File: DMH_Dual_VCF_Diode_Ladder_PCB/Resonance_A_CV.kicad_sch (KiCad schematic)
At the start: 24 parts, among them Q1 BC548, Q2 BC548, U3 TL074

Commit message: Reannotated whole schematic
OpAmp annotation is still tentative.
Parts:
- removed R27, R28, R31: 20k, Resistor_THT:R_Axial_DIN0207_L6.3mm_D2.5mm_P7.62mm_Horizontal, symbol Device:R_US
- removed R29, R35, R37, R38, R39, R44: 100k, Resistor_THT:R_Axial_DIN0207_L6.3mm_D2.5mm_P7.62mm_Horizontal, symbol Device:R_US
- removed R30, R34, R42: 10k, Resistor_THT:R_Axial_DIN0207_L6.3mm_D2.5mm_P7.62mm_Horizontal, symbol Device:R_US
- removed R33: 1k, Resistor_THT:R_Axial_DIN0207_L6.3mm_D2.5mm_P7.62mm_Horizontal, symbol Device:R_US
- removed R36: 33k, Resistor_THT:R_Axial_DIN0207_L6.3mm_D2.5mm_P7.62mm_Horizontal, symbol Device:R_US
- removed R40, R41: 100R, Resistor_THT:R_Axial_DIN0207_L6.3mm_D2.5mm_P7.62mm_Horizontal, symbol Device:R_US
- removed R43: 82k, Resistor_THT:R_Axial_DIN0207_L6.3mm_D2.5mm_P7.62mm_Horizontal, symbol Device:R_US
- removed RV10: 100k, Potentiometer_THT:Potentiometer_Bourns_3296W_Vertical, symbol Device:R_Potentiometer_Trim_US
- removed RV11: 100k, SynthStuff:Potentiometer_TT_P110KH1, symbol Device:R_Potentiometer_US
- removed RV8: 100k, SynthStuff:Potentiometer_Alpha_RD901F-40-00D_Single_Vertical, symbol Device:R_Potentiometer_US
- removed RV9: 50k, Potentiometer_THT:Potentiometer_Bourns_3296W_Vertical, symbol Device:R_Potentiometer_Trim_US
- removed U3: TL074, Package_DIP:DIP-14_W7.62mm_Socket, symbol Amplifier_Operational:TL074
- added R62: 33k, Resistor_THT:R_Axial_DIN0207_L6.3mm_D2.5mm_P7.62mm_Horizontal, symbol Device:R_US
- added R63, R72, R73: 20k, Resistor_THT:R_Axial_DIN0207_L6.3mm_D2.5mm_P7.62mm_Horizontal, symbol Device:R_US
- added R64, R65, R67, R71, R76, R77: 100k, Resistor_THT:R_Axial_DIN0207_L6.3mm_D2.5mm_P7.62mm_Horizontal, symbol Device:R_US
- added R66: 82k, Resistor_THT:R_Axial_DIN0207_L6.3mm_D2.5mm_P7.62mm_Horizontal, symbol Device:R_US
- added R68, R70: 100R, Resistor_THT:R_Axial_DIN0207_L6.3mm_D2.5mm_P7.62mm_Horizontal, symbol Device:R_US
- added R69, R74, R75: 10k, Resistor_THT:R_Axial_DIN0207_L6.3mm_D2.5mm_P7.62mm_Horizontal, symbol Device:R_US
- added R78: 1k, Resistor_THT:R_Axial_DIN0207_L6.3mm_D2.5mm_P7.62mm_Horizontal, symbol Device:R_US
- added RV16: 100k, SynthStuff:Potentiometer_TT_P110KH1, symbol Device:R_Potentiometer_US
- added RV17: 50k, Potentiometer_THT:Potentiometer_Bourns_3296W_Vertical, symbol Device:R_Potentiometer_Trim_US
- added RV18: 100k, SynthStuff:Potentiometer_Alpha_RD901F-40-00D_Single_Vertical, symbol Device:R_Potentiometer_US
- added RV19: 100k, Potentiometer_THT:Potentiometer_Bourns_3296W_Vertical, symbol Device:R_Potentiometer_Trim_US
- added U3, U4: TL074, Package_DIP:DIP-14_W7.62mm_Socket, symbol Amplifier_Operational:TL074
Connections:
- net +12V: now also R63.2, R72.2, R73.2, RV19.3
- net -12V: now also RV19.1
- net GND: now also R68.1, R70.1, R76.2, RV16.1, RV18.1, U4.12 (+)
- net Input: now also R67.2
- net Output: now also R78.1
- net Res CV Input: now also R62.1, RV16.3
- net at Q2.1 (C): now also R73.1, R75.2
- net at Q1.2 (B): now also R67.1, R68.2
- net at Q1.3 (E), Q2.3 (E): now also R69.2
- net at Q2.2 (B): now also R70.2, R71.2
- net at Q1.1 (C): now also R72.1, R74.2
- new net: R64.2, R65.2, R66.1, U4.13 (-)
- new net: R66.2, R69.1, U4.14
- new net: R62.2, RV17.1, U3.2 (-)
- new net: R64.1, RV17.2, RV17.3, U3.1
- new net: R65.1, RV18.2
- new net: R75.1, R76.1, U4.10 (+)
- new net: R77.1, R78.2, U4.8
- new net: R71.1, RV19.2
- new net: R74.1, R77.2, U4.9 (-)
- new net: RV16.2, U3.3 (+)
- new net: R63.1, RV18.3

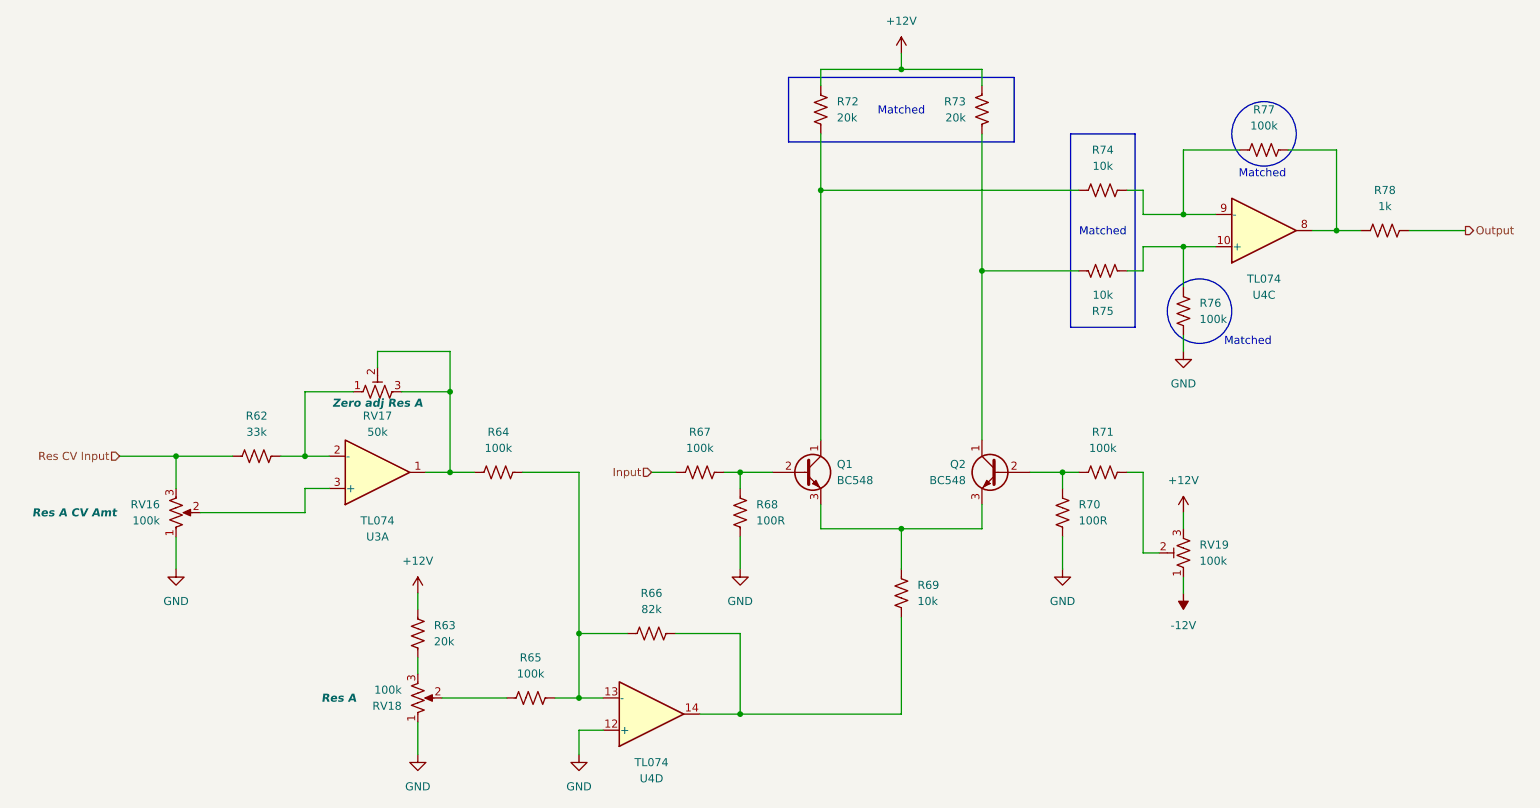
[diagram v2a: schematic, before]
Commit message: Reannotated OpAmps and cleared errors
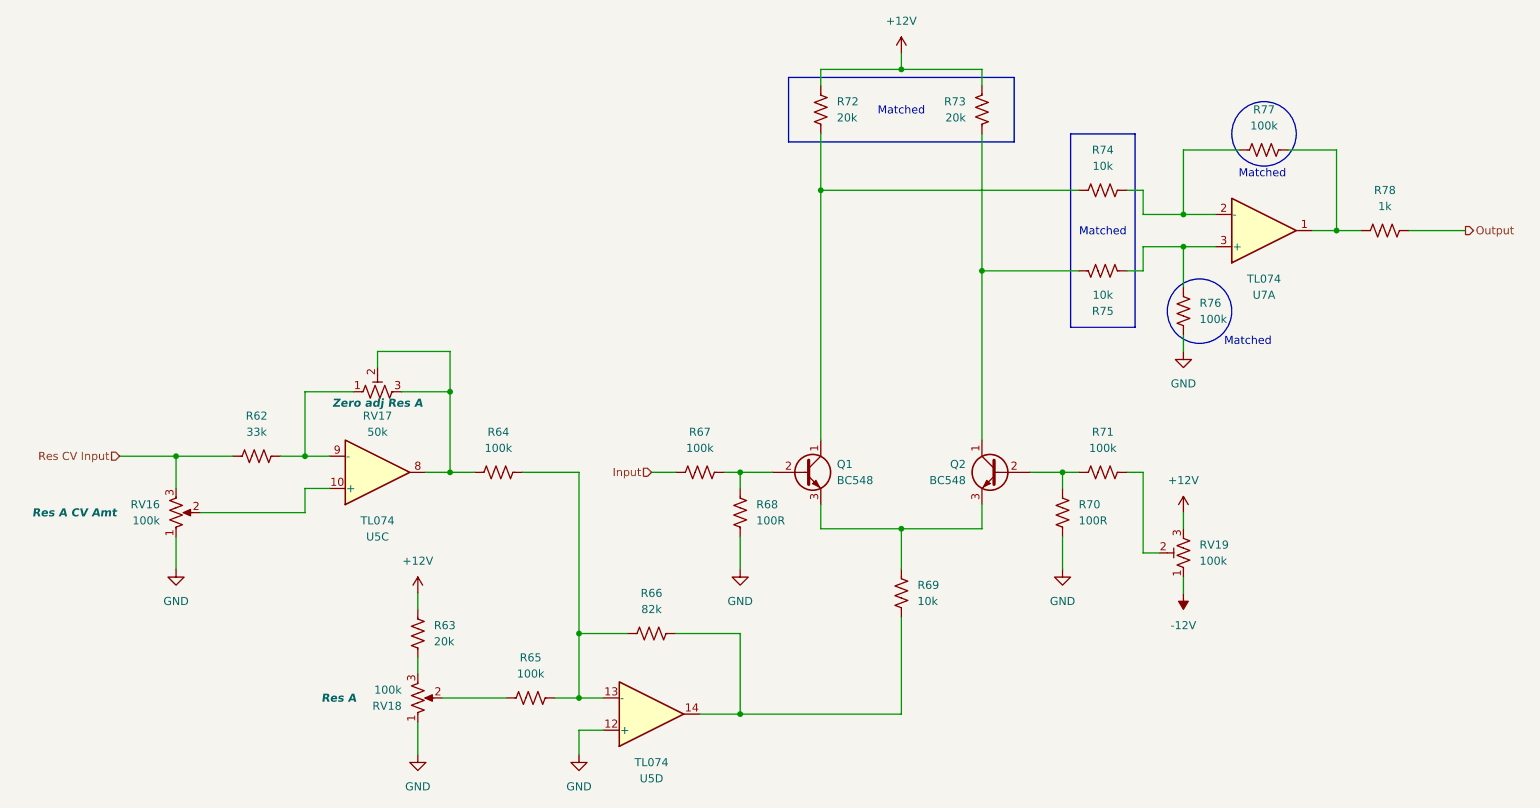
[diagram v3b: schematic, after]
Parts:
- renumbered U4 to U5, U3 to U5, U4 to U7
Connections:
- net at R62.2, RV17.1: now also U5.9 (-); no longer U5.2 (-)
- net at R64.1, RV17.2, RV17.3: now also U5.8; no longer U5.1
- net at R75.1, R76.1: now also U7.3 (+); no longer U7.10 (+)
- net at R77.1, R78.2: now also U7.1; no longer U7.8
- net at R74.1, R77.2: now also U7.2 (-); no longer U7.9 (-)
- net at RV16.2: now also U5.10 (+); no longer U5.3 (+)
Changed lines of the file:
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@@
 		(on_board yes)
 		(dnp no)
-		(property "Reference" "U4"
+		(property "Reference" "U5"
 			(at 138.43 137.16 0)
 			(effects
@@
 			(project "DMH_Dual_VCF_Diode_Ladder_PCB"
 				(path "/58f4306d-5387-4983-bb08-41a2313fd315/ad5c5475-8483-41b0-97cc-617422d54799"
-					(reference "U4")
+					(reference "U5")
 					(unit 4)
 				)
@@
 		(at 234.95 50.8 0)
 		(mirror x)
-		(unit 3)
-		(exclude_from_sim no)
-		(in_bom yes)
-		(on_board yes)
-		(dnp no)
-		(property "Reference" "U4"
+		(unit 1)
+		(exclude_from_sim no)
+		(in_bom yes)
+		(on_board yes)
+		(dnp no)
+		(property "Reference" "U7"
 			(at 234.95 60.96 0)
 			(effects
@@
 			(project "DMH_Dual_VCF_Diode_Ladder_PCB"
 				(path "/58f4306d-5387-4983-bb08-41a2313fd315/ad5c5475-8483-41b0-97cc-617422d54799"
-					(reference "U4")
-					(unit 3)
+					(reference "U7")
+					(unit 1)
 				)
 			)
@@
 		(at 95.25 88.9 0)
 		(mirror x)
-		(unit 1)
-		(exclude_from_sim no)
-		(in_bom yes)
-		(on_board yes)
-		(dnp no)
-		(property "Reference" "U3"
+		(unit 3)
+		(exclude_from_sim no)
+		(in_bom yes)
+		(on_board yes)
+		(dnp no)
+		(property "Reference" "U5"
 			(at 95.25 99.06 0)
 			(effects
@@
 			(project "DMH_Dual_VCF_Diode_Ladder_PCB"
 				(path "/58f4306d-5387-4983-bb08-41a2313fd315/ad5c5475-8483-41b0-97cc-617422d54799"
-					(reference "U3")
-					(unit 1)
-				)
-			)
+					(reference "U5")
+					(unit 3)
+				)
+			)

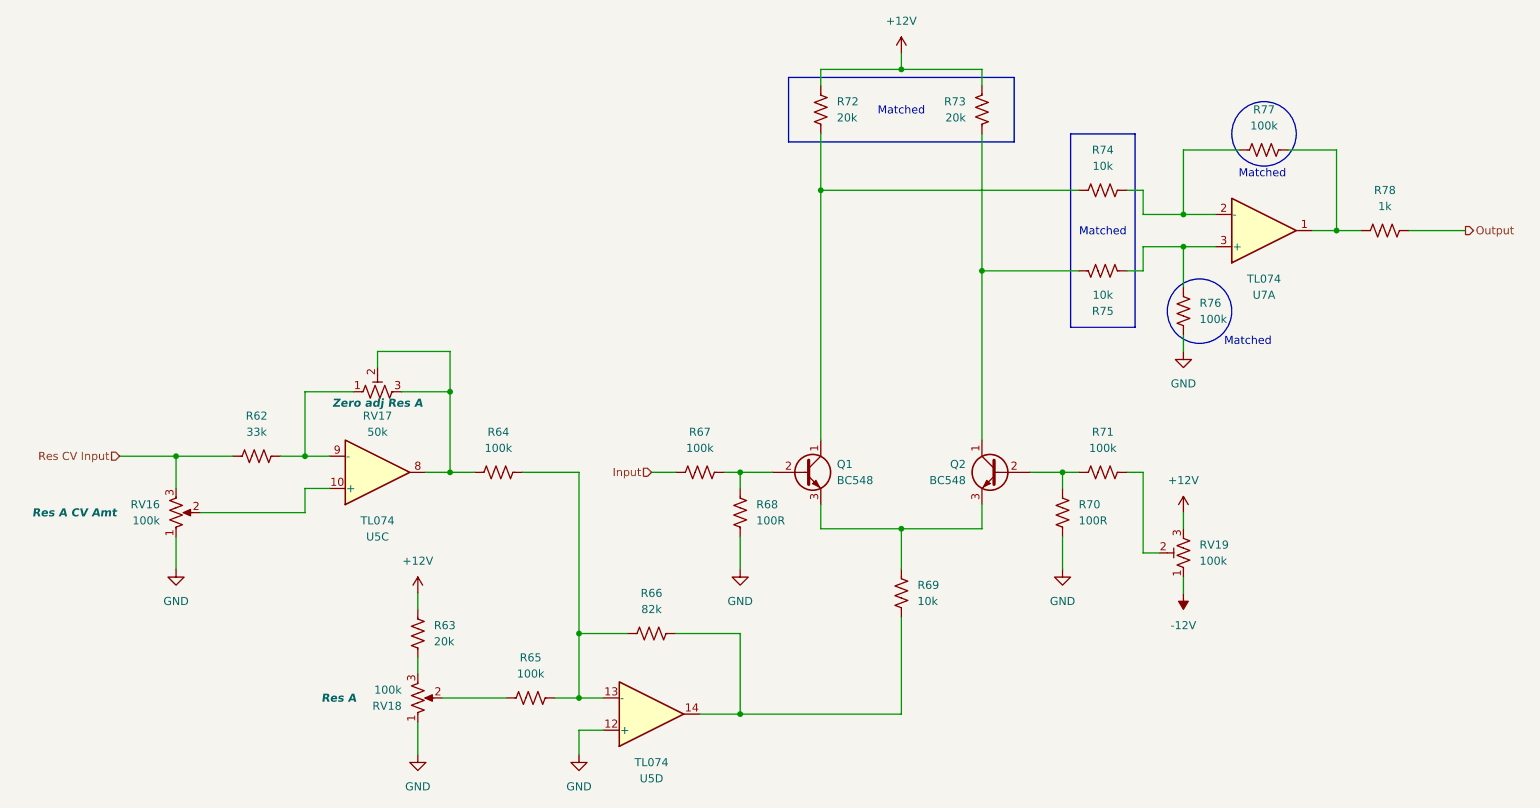
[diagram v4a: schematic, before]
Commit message: Re-annotated OpAmps as per PCB layout
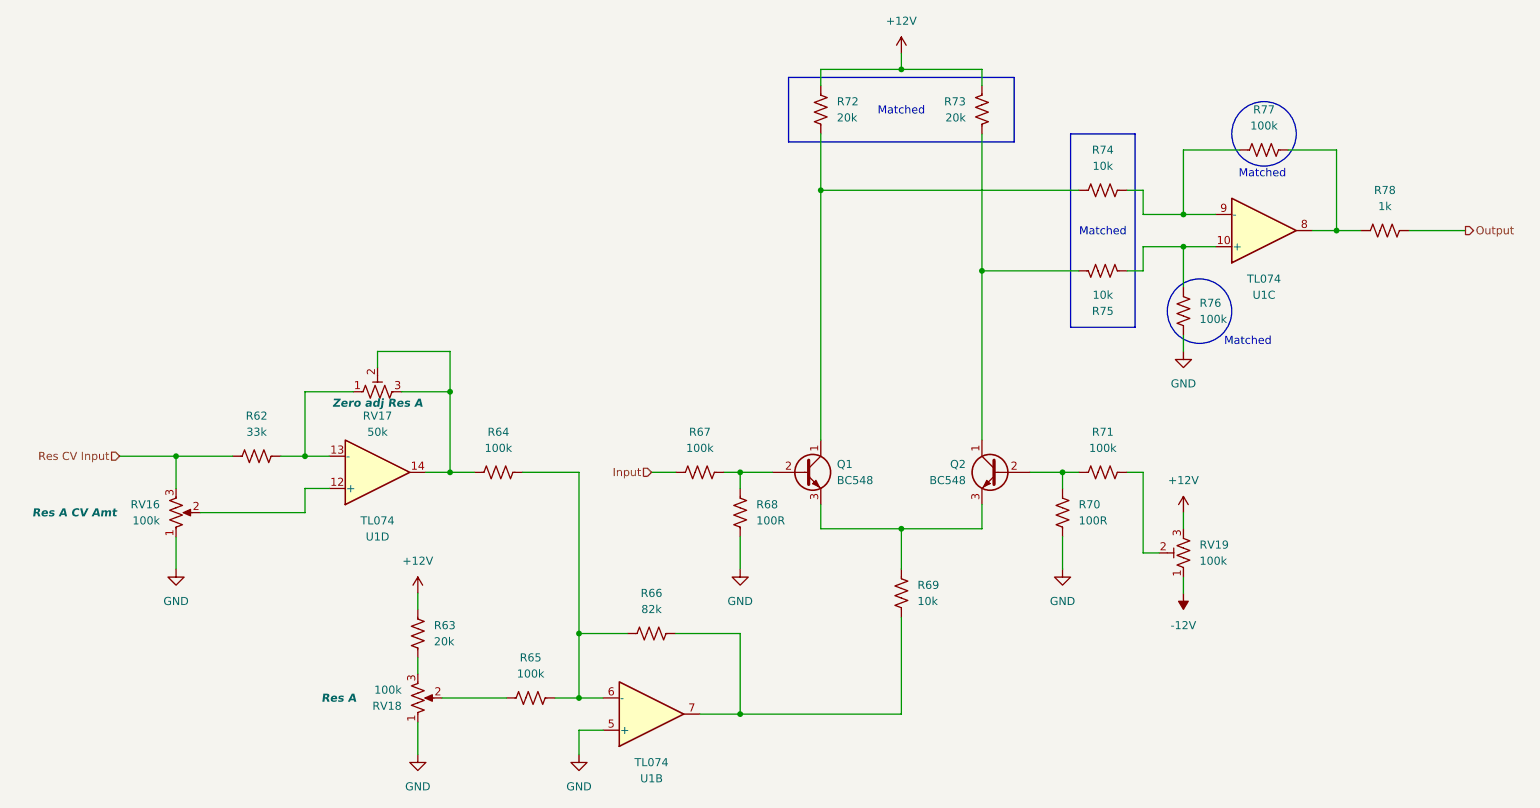
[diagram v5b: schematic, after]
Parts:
- renumbered U5 to U1, U7 to U1
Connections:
- net GND: now also U1.5 (+); no longer U1.12 (+)
- net at R64.2, R65.2, R66.1: now also U1.6 (-); no longer U1.13 (-)
- net at R66.2, R69.1: now also U1.7; no longer U1.14
- net at R62.2, RV17.1: now also U1.13 (-); no longer U1.9 (-)
- net at R64.1, RV17.2, RV17.3: now also U1.14; no longer U1.8
- net at R75.1, R76.1: now also U1.10 (+); no longer U1.3 (+)
- net at R77.1, R78.2: now also U1.8; no longer U1.1
- net at R74.1, R77.2: now also U1.9 (-); no longer U1.2 (-)
- net at RV16.2: now also U1.12 (+); no longer U1.10 (+)
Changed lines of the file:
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@@
 		(at 138.43 127 0)
 		(mirror x)
-		(unit 4)
-		(exclude_from_sim no)
-		(in_bom yes)
-		(on_board yes)
-		(dnp no)
-		(property "Reference" "U5"
+		(unit 2)
+		(exclude_from_sim no)
+		(in_bom yes)
+		(on_board yes)
+		(dnp no)
+		(property "Reference" "U1"
 			(at 138.43 137.16 0)
 			(effects
@@
 			(project "DMH_Dual_VCF_Diode_Ladder_PCB"
 				(path "/58f4306d-5387-4983-bb08-41a2313fd315/ad5c5475-8483-41b0-97cc-617422d54799"
-					(reference "U5")
-					(unit 4)
+					(reference "U1")
+					(unit 2)
 				)
 			)
@@
 		(at 234.95 50.8 0)
 		(mirror x)
-		(unit 1)
-		(exclude_from_sim no)
-		(in_bom yes)
-		(on_board yes)
-		(dnp no)
-		(property "Reference" "U7"
+		(unit 3)
+		(exclude_from_sim no)
+		(in_bom yes)
+		(on_board yes)
+		(dnp no)
+		(property "Reference" "U1"
 			(at 234.95 60.96 0)
 			(effects
@@
 			(project "DMH_Dual_VCF_Diode_Ladder_PCB"
 				(path "/58f4306d-5387-4983-bb08-41a2313fd315/ad5c5475-8483-41b0-97cc-617422d54799"
-					(reference "U7")
-					(unit 1)
+					(reference "U1")
+					(unit 3)
 				)
 			)
@@
 		(at 95.25 88.9 0)
 		(mirror x)
-		(unit 3)
-		(exclude_from_sim no)
-		(in_bom yes)
-		(on_board yes)
-		(dnp no)
-		(property "Reference" "U5"
+		(unit 4)
+		(exclude_from_sim no)
+		(in_bom yes)
+		(on_board yes)
+		(dnp no)
+		(property "Reference" "U1"
 			(at 95.25 99.06 0)
 			(effects
@@
 			(project "DMH_Dual_VCF_Diode_Ladder_PCB"
 				(path "/58f4306d-5387-4983-bb08-41a2313fd315/ad5c5475-8483-41b0-97cc-617422d54799"
-					(reference "U5")
-					(unit 3)
-				)
-			)
+					(reference "U1")
+					(unit 4)
+				)
+			)
